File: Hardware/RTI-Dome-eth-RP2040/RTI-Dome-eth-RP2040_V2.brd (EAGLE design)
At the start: 111.1 x 76.3 mm, 106 parts, among them IC1 REG1117FA-5.0_500, IC2 24LC64T-I/SN, IC3 FT232RL, IC4 RASPBERRY_PI_PICO, IC8 REG1117-3.3V, J2 XT60PW-M, T1 MMBT3904LT1, T2 MMBT3904LT1, T3 MMBT3904LT1, U1 W5500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

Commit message: Fixed board for W5500 Int.
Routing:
- net INT_N: track 73.0 -> 56.9 mm, vias 2 -> 6
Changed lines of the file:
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@@
 <contactref element="U$1" pad="P$10"/>
 <contactref element="U$1" pad="P$5"/>
-<via x="46.355" y="51.435" extent="1-16" drill="0.5" diameter="1.27"/>
+<via x="46.99" y="50.165" extent="1-16" drill="0.5" diameter="1.27"/>
 <contactref element="IC1" pad="1"/>
 <contactref element="C27" pad="2"/>
@@
 <via x="76.835" y="12.7" extent="1-16" drill="0.5" diameter="1.27"/>
 <via x="63.5" y="20.32" extent="1-16" drill="0.5" diameter="1.27"/>
+<via x="52.705" y="58.42" extent="1-16" drill="0.5" diameter="1.27"/>
+<via x="39.37" y="55.245" extent="1-16" drill="0.35"/>
 </signal>
 <signal name="+12V" class="1">
@@
 <wire x1="60.96" y1="38.965" x2="60.96" y2="38.735" width="0.254" layer="1"/>
 <via x="60.96" y="38.735" extent="1-16" drill="0.35"/>
-<via x="56.515" y="52.705" extent="1-16" drill="0.35"/>
-<wire x1="56.515" y1="57.15" x2="56.515" y2="52.705" width="0.254" layer="1"/>
-<wire x1="56.515" y1="57.15" x2="51.435" y2="62.23" width="0.254" layer="1"/>
-<wire x1="33.655" y1="62.23" x2="33.02" y2="61.595" width="0.254" layer="1"/>
-<wire x1="51.435" y1="62.23" x2="45.50513125" y2="62.23" width="0.254" layer="1"/>
-<wire x1="45.50513125" y1="62.23" x2="45.36573125" y2="62.3694" width="0.254" layer="1"/>
-<wire x1="45.36573125" y1="62.3694" x2="43.53426875" y2="62.3694" width="0.254" layer="1"/>
-<wire x1="43.53426875" y1="62.3694" x2="43.39486875" y2="62.23" width="0.254" layer="1"/>
-<wire x1="43.39486875" y1="62.23" x2="33.655" y2="62.23" width="0.254" layer="1"/>
-<wire x1="33.02" y1="61.595" x2="33.02" y2="57.785" width="0.254" layer="1"/>
-<wire x1="33.02" y1="57.785" x2="32.0294" y2="56.7944" width="0.254" layer="1"/>
-<wire x1="32.0294" y1="56.7944" x2="31.3712375" y2="56.7944" width="0.254" layer="1"/>
-<wire x1="29.1868375" y1="54.61" x2="22.86" y2="54.61" width="0.254" layer="1"/>
-<wire x1="31.3712375" y1="56.7944" x2="29.1868375" y2="54.61" width="0.254" layer="1"/>
-<wire x1="22.86" y1="54.61" x2="21.59" y2="55.88" width="0.254" layer="1"/>
-<wire x1="21.59" y1="55.88" x2="21.59" y2="60.49" width="0.254" layer="1"/>
 <wire x1="60.96" y1="38.735" x2="56.515" y2="38.735" width="0.254" layer="16"/>
 <wire x1="56.515" y1="38.735" x2="55.245" y2="40.005" width="0.254" layer="16"/>
-<wire x1="55.245" y1="40.005" x2="55.245" y2="51.435" width="0.254" layer="16"/>
-<wire x1="55.245" y1="51.435" x2="56.515" y2="52.705" width="0.254" layer="16"/>
+<wire x1="55.245" y1="40.005" x2="55.245" y2="46.355" width="0.254" layer="16"/>
+<wire x1="50.165" y1="51.435" x2="45.72" y2="51.435" width="0.254" layer="16"/>
+<wire x1="55.245" y1="46.355" x2="50.165" y2="51.435" width="0.254" layer="16"/>
+<via x="45.72" y="51.435" extent="1-16" drill="0.35"/>
+<wire x1="45.72" y1="51.435" x2="42.926" y2="51.435" width="0.254" layer="1"/>
+<via x="42.926" y="51.435" extent="1-16" drill="0.35"/>
+<wire x1="42.926" y1="51.435" x2="39.37" y2="51.435" width="0.254" layer="16"/>
+<via x="39.37" y="51.435" extent="1-16" drill="0.35"/>
+<wire x1="39.37" y1="51.435" x2="34.29" y2="51.435" width="0.254" layer="1"/>
+<via x="34.29" y="51.435" extent="1-16" drill="0.35"/>
+<wire x1="34.29" y1="51.435" x2="30.48" y2="51.435" width="0.254" layer="16"/>
+<via x="30.48" y="51.435" extent="1-16" drill="0.35"/>
+<wire x1="30.48" y1="51.435" x2="24.765" y2="51.435" width="0.254" layer="1"/>
+<wire x1="24.765" y1="51.435" x2="21.59" y2="54.61" width="0.254" layer="1"/>
+<wire x1="21.59" y1="54.61" x2="21.59" y2="60.49" width="0.254" layer="1"/>
 </signal>
 <signal name="N$17">
@@
 <wire x1="56.29275" y1="34.70275" x2="57.15" y2="35.56" width="0.254" layer="1"/>
 <wire x1="57.15" y1="35.56" x2="60.325" y2="35.56" width="0.254" layer="1"/>
-<wire x1="36.83" y1="60.49" x2="36.83" y2="57.15" width="0.254" layer="1"/>
-<wire x1="36.83" y1="57.15" x2="40.005" y2="53.975" width="0.254" layer="1"/>
-<wire x1="40.005" y1="53.975" x2="51.435" y2="42.545" width="0.254" layer="1"/>
 <wire x1="51.435" y1="42.545" x2="51.435" y2="36.83" width="0.254" layer="1"/>
 <via x="51.435" y="36.83" extent="1-16" drill="0.35"/>
@@
 <wire x1="52.705" y1="35.56" x2="57.15" y2="35.56" width="0.254" layer="16"/>
 <via x="57.15" y="35.56" extent="1-16" drill="0.35"/>
+<wire x1="47.625" y1="45.72" x2="48.26" y2="45.72" width="0.254" layer="1"/>
+<wire x1="48.26" y1="45.72" x2="51.435" y2="42.545" width="0.254" layer="1"/>
+<wire x1="36.83" y1="56.515" x2="47.625" y2="45.72" width="0.254" layer="1"/>
+<wire x1="36.83" y1="60.49" x2="36.83" y2="56.515" width="0.254" layer="1"/>
 </signal>
 <signal name="RESET">
@@
 <wire x1="33.02" y1="64.455" x2="33.02" y2="62.865" width="0.254" layer="1"/>
 <via x="33.02" y="62.865" extent="1-16" drill="0.35"/>
-<wire x1="33.02" y1="62.865" x2="38.7632" y2="57.1218" width="0.254" layer="16"/>
+<wire x1="33.02" y1="62.865" x2="40.0332" y2="55.8518" width="0.254" layer="16"/>
 <wire x1="49.1744" y1="29.4662375" x2="49.166" y2="29.4578375" width="0.254" layer="16"/>
 <wire x1="49.166" y1="29.4578375" x2="49.166" y2="28.956" width="0.254" layer="16"/>
-<wire x1="38.7632" y1="57.1218" x2="38.7632" y2="56.5470625" width="0.254" layer="16"/>
-<wire x1="38.7632" y1="56.5470625" x2="49.1744" y2="46.1358625" width="0.254" layer="16"/>
+<wire x1="40.0332" y1="55.8518" x2="40.0332" y2="55.2770625" width="0.254" layer="16"/>
+<wire x1="40.0332" y1="55.2770625" x2="49.1744" y2="46.1358625" width="0.254" layer="16"/>
 <wire x1="49.1744" y1="46.1358625" x2="49.1744" y2="29.4662375" width="0.254" layer="16"/>
 <contactref element="U$3" pad="P$6"/>

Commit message: Added a few things to the V2 board
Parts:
- added Q1: DMG2305UX-7, samacsys:SOT96P240X115-3N
- added S1: EVQ-P2H02B, samacsys:EVQP2H02B
- IC4: value RASPBERRY_PI_PICO -> RASPBERRY_PI_PICOW; device samacsys:RASPBERRYPIPICO -> samacsys:RASPBERRYPIPICO-W
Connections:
- new net VSYS: IC4.39, Q1.2
- net GND: now also S1.2, S1.4
- net RESET: now also S1.3
- net VBUS: now also Q1.1
- net VCC: now also Q1.3; no longer IC4.39
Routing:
- net RESET: track 0.00 -> 9.39 mm
- net VCC: track 231.6 -> 239.7 mm
- net VSYS: track 0.00 -> 2.67 mm
- net VBUS: track 0.00 -> 2.67 mm
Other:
- board text added: "Reset"
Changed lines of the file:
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@@
 <text x="32.665" y="74.06" size="0.6096" layer="22" rot="MR0">SPARE1</text>
 <hole x="107.315" y="71.755" drill="3.2"/>
-<text x="2.54" y="64.135" size="1.778" layer="51">Dome Rotator / RoR</text>
+<text x="58.42" y="57.785" size="1.778" layer="21">Dome Rotator / RoR</text>
 <hole x="107.315" y="21.59" drill="3.2"/>
 <wire x1="0" y1="75.01" x2="1.26" y2="76.27" width="0" layer="20" curve="-90"/>
@@
 <text x="40.005" y="8.255" size="0.6096" layer="21">GND</text>
 <text x="24.765" y="8.255" size="0.6096" layer="21">GND</text>
+<text x="7.62" y="64.77" size="1.778" layer="21">Reset</text>
 </plain>
 <attributes>
@@
 <attribute name="VALUE" x="79.92" y="30.605" size="1.27" layer="27"/>
 </element>
-<element name="J2" library="samacsys" library_urn="urn:adsk.eagle:library:37256869" package="XT60PWM" package3d_urn="urn:adsk.eagle:package:37256940/5" value="XT60PW-M" x="100.42" y="8.815" smashed="yes" rot="R270">
+<element name="J2" library="samacsys" library_urn="urn:adsk.eagle:library:37256869" package="XT60PWM" package3d_urn="urn:adsk.eagle:package:37256940/7" value="XT60PW-M" x="100.42" y="8.815" smashed="yes" rot="R270">
 <attribute name="ARROW_PART_NUMBER" value="" x="100.42" y="8.815" size="1.778" layer="27" rot="R270" display="off"/>
 <attribute name="ARROW_PRICE-STOCK" value="" x="100.42" y="8.815" size="1.778" layer="27" rot="R270" display="off"/>
@@
 <attribute name="VALUE" x="67.945" y="62.23" size="1.27" layer="27"/>
 </element>
-<element name="IC4" library="samacsys" library_urn="urn:adsk.eagle:library:37256869" package="RASPBERRYPIPICO" package3d_urn="urn:adsk.eagle:package:40546189/7" value="RASPBERRY_PI_PICO" x="25.4" y="50.8" smashed="yes" rot="R90">
-<attribute name="ARROW_PART_NUMBER" value="" x="25.4" y="50.8" size="1.778" layer="27" rot="R90" display="off"/>
-<attribute name="ARROW_PRICE-STOCK" value="" x="25.4" y="50.8" size="1.778" layer="27" rot="R90" display="off"/>
-<attribute name="DESCRIPTION" value="RASPBERRY-PI - RASPBERRY PI PICO - Raspberry Pi Board, Raspberry Pi Pic, RP2040, 32bit, ARM Cortex-M0+" x="25.4" y="50.8" size="1.778" layer="27" rot="R90" display="off"/>
-<attribute name="HEIGHT" value="1mm" x="25.4" y="50.8" size="1.778" layer="27" rot="R90" display="off"/>
+<element name="IC4" library="samacsys" library_urn="urn:adsk.eagle:library:37256869" package="RASPBERRYPIPICO-W" package3d_urn="urn:adsk.eagle:package:44159720/2" value="RASPBERRY_PI_PICOW" x="25.4" y="50.8" smashed="yes" rot="R90">
 <attribute name="JLCPCBPN" value="C7203003" x="25.4" y="50.8" size="1.778" layer="27" rot="R90" display="off"/>
-<attribute name="MANUFACTURER_NAME" value="RASPBERRY-PI PICO" x="25.4" y="50.8" size="1.778" layer="27" rot="R90" display="off"/>
-<attribute name="MANUFACTURER_PART_NUMBER" value="SC0916" x="25.4" y="50.8" size="1.778" layer="27" rot="R90" display="off"/>
-<attribute name="MOUSER_PART_NUMBER" value="SC0915" x="25.4" y="50.8" size="1.778" layer="27" rot="R90" display="off"/>
-<attribute name="MOUSER_PRICE-STOCK" value="" x="25.4" y="50.8" size="1.778" layer="27" rot="R90" display="off"/>
-<attribute name="MPN" value="SC0916" x="25.4" y="50.8" size="1.778" layer="27" rot="R90" display="off"/>
 <attribute name="NAME" x="25.4" y="46.99" size="0.635" layer="25" rot="R180"/>
-<attribute name="PARTNUMBER" value="SCO918" x="25.4" y="50.8" size="1.778" layer="27" rot="R90" display="off"/>
 <attribute name="VALUE" x="25.4" y="53.975" size="0.635" layer="27" rot="R180"/>
 </element>
@@
 <attribute name="NAME" x="80.645" y="29.7" size="1.27" layer="25" align="center"/>
 <attribute name="VALUE" x="81.28" y="17" size="1.27" layer="27" align="center"/>
+</element>
+<element name="S1" library="samacsys" library_urn="urn:adsk.eagle:library:37256869" package="EVQP2H02B" package3d_urn="urn:adsk.eagle:package:44159643/2" value="EVQ-P2H02B" x="18.415" y="65.405" smashed="yes" rot="R90">
+<attribute name="ARROW_PART_NUMBER" value="EVQ-P2H02B" x="18.415" y="65.405" size="1.778" layer="27" rot="R90" display="off"/>
+<attribute name="ARROW_PRICE-STOCK" value="https://www.arrow.com/en/products/evq-p2h02b/panasonic?region=nac" x="18.415" y="65.405" size="1.778" layer="27" rot="R90" display="off"/>
+<attribute name="DESCRIPTION" value="Tactile Switches 2.5NF 4.7x3.5x2.5mm" x="18.415" y="65.405" size="1.778" layer="27" rot="R90" display="off"/>
+<attribute name="HEIGHT" value="2.7mm" x="18.415" y="65.405" size="1.778" layer="27" rot="R90" display="off"/>
+<attribute name="MANUFACTURER_NAME" value="Panasonic" x="18.415" y="65.405" size="1.778" layer="27" rot="R90" display="off"/>
+<attribute name="MANUFACTURER_PART_NUMBER" value="EVQ-P2H02B" x="18.415" y="65.405" size="1.778" layer="27" rot="R90" display="off"/>
+<attribute name="MOUSER_PART_NUMBER" value="667-EVQ-P2H02B" x="18.415" y="65.405" size="1.778" layer="27" rot="R90" display="off"/>
+<attribute name="MOUSER_PRICE-STOCK" value="https://www.mouser.co.uk/ProductDetail/Panasonic/EVQ-P2H02B?qs=WwqriLBepZtQ2aXTL4JXCg%3D%3D" x="18.415" y="65.405" size="1.778" layer="27" rot="R90" display="off"/>
+<attribute name="NAME" x="18.165" y="65.405" size="1.27" layer="25" rot="R90" align="center"/>
+<attribute name="VALUE" x="18.165" y="65.405" size="1.27" layer="27" rot="R90" align="center"/>
+</element>
+<element name="Q1" library="samacsys" library_urn="urn:adsk.eagle:library:37256869" package="SOT96P240X115-3N" package3d_urn="urn:adsk.eagle:package:44159710/2" value="DMG2305UX-7" x="2.54" y="64.135" smashed="yes" rot="R90">
+<attribute name="ARROW_PART_NUMBER" value="DMG2305UX-7" x="2.54" y="64.135" size="1.778" layer="27" rot="R90" display="off"/>
+<attribute name="ARROW_PRICE-STOCK" value="https://www.arrow.com/en/products/dmg2305ux-7/diodes-incorporated?region=nac" x="2.54" y="64.135" size="1.778" layer="27" rot="R90" display="off"/>
+<attribute name="DESCRIPTION" value="MOSFET P-Ch 20V 5A Enhancement SOT23 Diodes Inc DMG2305UX-7 P-channel MOSFET Transistor, -3.3 A, -20 V, 3-Pin SOT-23" x="2.54" y="64.135" size="1.778" layer="27" rot="R90" display="off"/>
+<attribute name="HEIGHT" value="1.15mm" x="2.54" y="64.135" size="1.778" layer="27" rot="R90" display="off"/>
+<attribute name="MANUFACTURER_NAME" value="Diodes Incorporated" x="2.54" y="64.135" size="1.778" layer="27" rot="R90" display="off"/>
+<attribute name="MANUFACTURER_PART_NUMBER" value="DMG2305UX-7" x="2.54" y="64.135" size="1.778" layer="27" rot="R90" display="off"/>
+<attribute name="MOUSER_PART_NUMBER" value="621-DMG2305UX-7" x="2.54" y="64.135" size="1.778" layer="27" rot="R90" display="off"/>
+<attribute name="MOUSER_PRICE-STOCK" value="https://www.mouser.co.uk/ProductDetail/Diodes-Incorporated/DMG2305UX-7?qs=L1DZKBg7t5F%2FNBHrjfxC%252Bg%3D%3D" x="2.54" y="64.135" size="1.778" layer="27" rot="R90" display="off"/>
+<attribute name="NAME" x="0" y="64.135" size="1.27" layer="25" rot="R90" align="center"/>
+<attribute name="VALUE" x="5.08" y="64.135" size="1.27" layer="27" rot="R90" align="center"/>
 </element>
 </elements>
@@
 <via x="52.705" y="58.42" extent="1-16" drill="0.5" diameter="1.27"/>
 <via x="39.37" y="55.245" extent="1-16" drill="0.35"/>
+<contactref element="S1" pad="2"/>
+<contactref element="S1" pad="4"/>
 </signal>
 <signal name="+12V" class="1">
@@
 <contactref element="R9" pad="1"/>
 <contactref element="R4" pad="2"/>
-<contactref element="IC4" pad="39"/>
 <wire x1="57.15" y1="19.47" x2="63.285" y2="13.335" width="1.27" layer="1"/>
 <wire x1="72.1614" y1="18.4404" x2="72.1614" y2="15.2654" width="1.27" layer="1"/>
@@
 <via x="41.115" y="12.54" extent="1-16" drill="0.35"/>
 <wire x1="40.64" y1="12.065" x2="41.115" y2="12.54" width="0.6096" layer="16"/>
-<wire x1="3.81" y1="60.49" x2="3.81" y2="55.88" width="1.27" layer="1"/>
-<via x="3.81" y="55.88" extent="1-16" drill="0.5" diameter="1.27"/>
-<wire x1="3.81" y1="55.88" x2="3.81" y2="14.605" width="1.27" layer="16"/>
+<via x="3.81" y="66.675" extent="1-16" drill="0.5" diameter="1.27"/>
+<wire x1="3.81" y1="66.675" x2="3.81" y2="14.605" width="1.27" layer="16"/>
 <contactref element="X6" pad="3"/>
 <contactref element="X2" pad="3"/>
@@
 <wire x1="95.84" y1="24.175" x2="81.28" y2="24.175" width="0.508" layer="1"/>
 <wire x1="96.94" y1="23.075" x2="95.84" y2="24.175" width="0.508" layer="1"/>
+<contactref element="Q1" pad="3"/>
+<wire x1="2.54" y1="65.235" x2="2.54" y2="65.405" width="1.27" layer="1"/>
+<wire x1="2.54" y1="65.405" x2="3.81" y2="66.675" width="1.27" layer="1"/>
 </signal>
 <signal name="N$2">
@@
 <signal name="RESET">
 <contactref element="IC4" pad="30"/>
+<contactref element="S1" pad="3"/>
+<wire x1="26.67" y1="60.49" x2="26.325" y2="60.835" width="0.254" layer="1"/>
+<wire x1="26.325" y1="64.3" x2="26.325" y2="60.835" width="0.254" layer="1"/>
+<wire x1="26.325" y1="64.3" x2="26.07" y2="64.555" width="0.254" layer="1"/>
+<wire x1="26.07" y1="64.555" x2="20.99" y2="64.555" width="0.254" layer="1"/>
 </signal>
 <signal name="AVDD">
@@
 <contactref element="IC4" pad="37"/>
 </signal>
-<signal name="VBUS">
-<contactref element="IC4" pad="40"/>
-</signal>
 <signal name="USB_VCC">
 <contactref element="X13" pad="1"/>
@@
 <wire x1="45.847" y1="8.532" x2="45.847" y2="3.6" width="0.4064" layer="1"/>
 </signal>
+<signal name="VBUS">
+<contactref element="IC4" pad="40"/>
+<contactref element="Q1" pad="1"/>
+<wire x1="1.27" y1="60.49" x2="1.27" y2="62.725" width="1.27" layer="1"/>
+<wire x1="1.27" y1="62.725" x2="1.58" y2="63.035" width="1.27" layer="1"/>
+</signal>
+<signal name="VSYS">
+<contactref element="Q1" pad="2"/>
+<contactref element="IC4" pad="39"/>
+<wire x1="3.81" y1="60.49" x2="3.81" y2="62.725" width="1.27" layer="1"/>
+<wire x1="3.81" y1="62.725" x2="3.5" y2="63.035" width="1.27" layer="1"/>
+</signal>
 </signals>

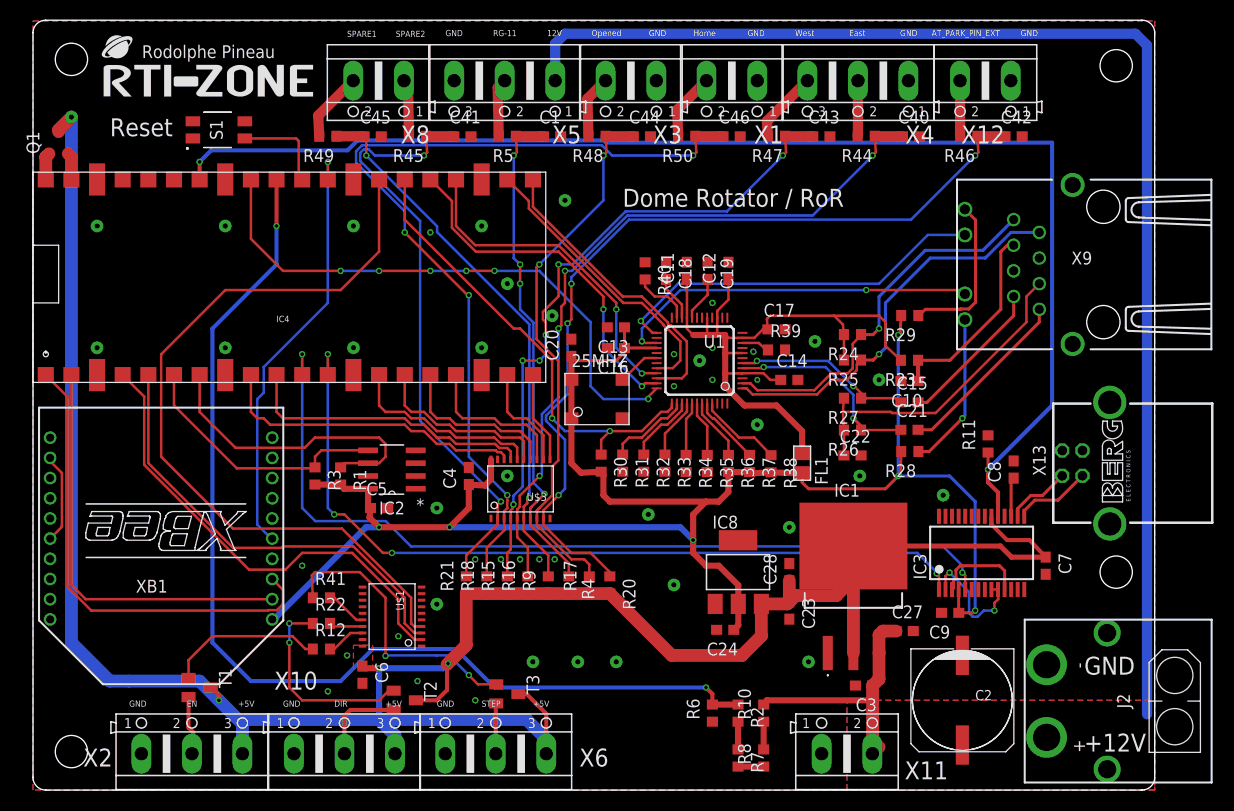
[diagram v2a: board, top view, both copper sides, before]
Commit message: Removed XBee from RP2040 boards as they'll use WiFi
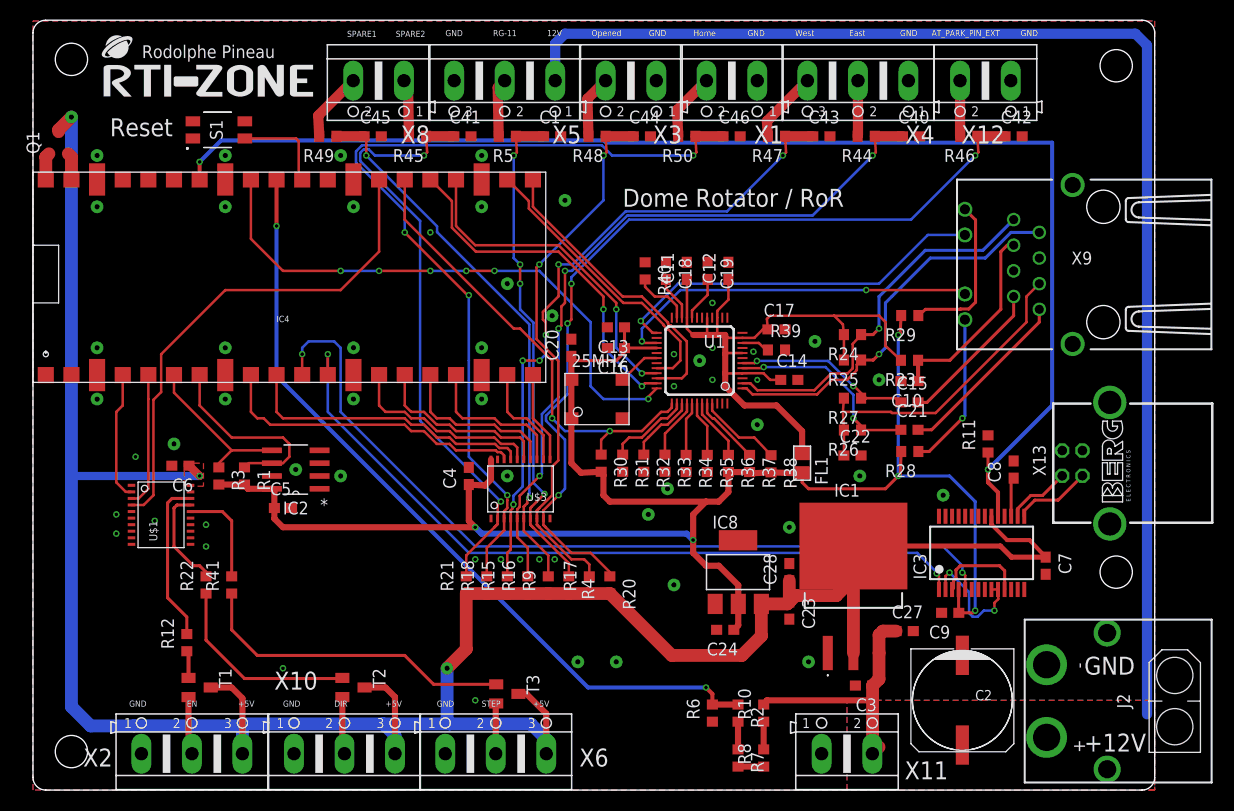
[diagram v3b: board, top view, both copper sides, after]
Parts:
- removed XB1: XBEE, rti:XBEE
- moved C6 27.5 mm to (14.6, 32.1), turned to 180 degrees
- moved U$1 25.0 mm to (12.7, 27.3), turned to 0 degrees
- moved R12 13.4 mm to (15.2, 14.6), turned to 90 degrees
- moved R22 12.0 mm to (17.1, 20.3), turned to 90 degrees
- moved IC2 9.53 mm to (26.0, 31.8)
- moved R1 9.53 mm to (21.0, 31.1)
- moved R3 9.53 mm to (18.4, 31.1)
- moved C5 9.52 mm to (24.8, 27.9)
- moved R41 8.98 mm to (19.7, 20.3), turned to 90 degrees
- moved T2 5.24 mm to (31.8, 10.2)
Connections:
- removed net N$9: XB1.12, XB1.16
- removed net XBEE_DIN: IC4.1, XB1.3
- removed net XBEE_DOUT: IC4.2, XB1.2
- new net RX: IC4.1
- new net TX: IC4.2
- net 3.3V: no longer XB1.1
- net GND: no longer XB1.10, XB1.9
- net XBEE_RESET: no longer XB1.5
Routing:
- net XBEE_DIN: track 47.4 -> 0.00 mm
- net XBEE_RESET: track 42.6 -> 0.00 mm, vias 1 -> 0
- net XBEE_DOUT: track 41.3 -> 0.00 mm
- net M_EN: track 47.2 -> 12.8 mm
- net M_DIR: track 44.4 -> 13.3 mm
- net M_STEP: track 77.4 -> 49.8 mm
- net VPIN: track 106.4 -> 79.3 mm
- net VCC: track 239.7 -> 259.3 mm, vias 4 -> 3
- net EN-5V_TR: track 15.6 -> 2.72 mm
- net M_EN_5V: track 3.88 -> 16.2 mm
- net SCL: track 30.4 -> 19.6 mm
- net SDA: track 26.2 -> 16.0 mm
- net N$9: track 8.97 -> 0.00 mm
- net M_DIR_5V: track 3.32 -> 10.2 mm
- net M_STEP_5V: track 4.13 -> 9.96 mm
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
